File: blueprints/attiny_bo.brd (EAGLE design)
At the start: 36 x 20 mm, 8 parts, among them IC1 ATTiny85, J1 AVR_SPI_PRG_6NS

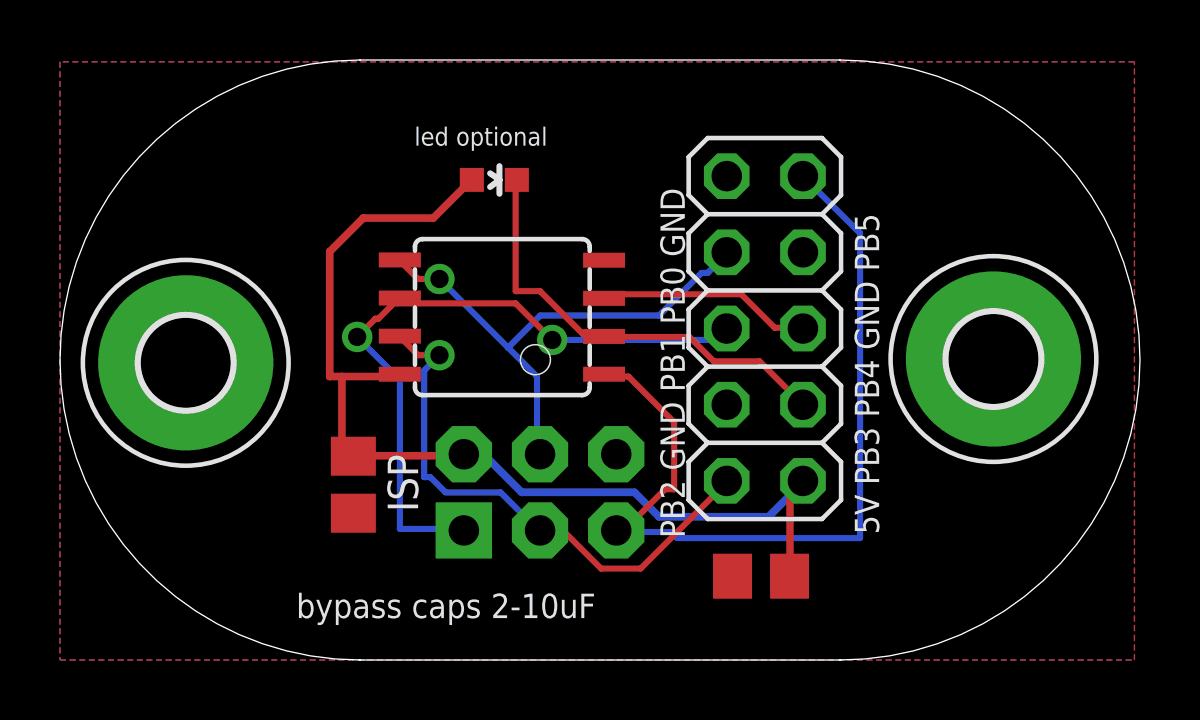
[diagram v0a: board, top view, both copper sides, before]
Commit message: rethought the signals to 5x2 header, tuned the mounting pad positions
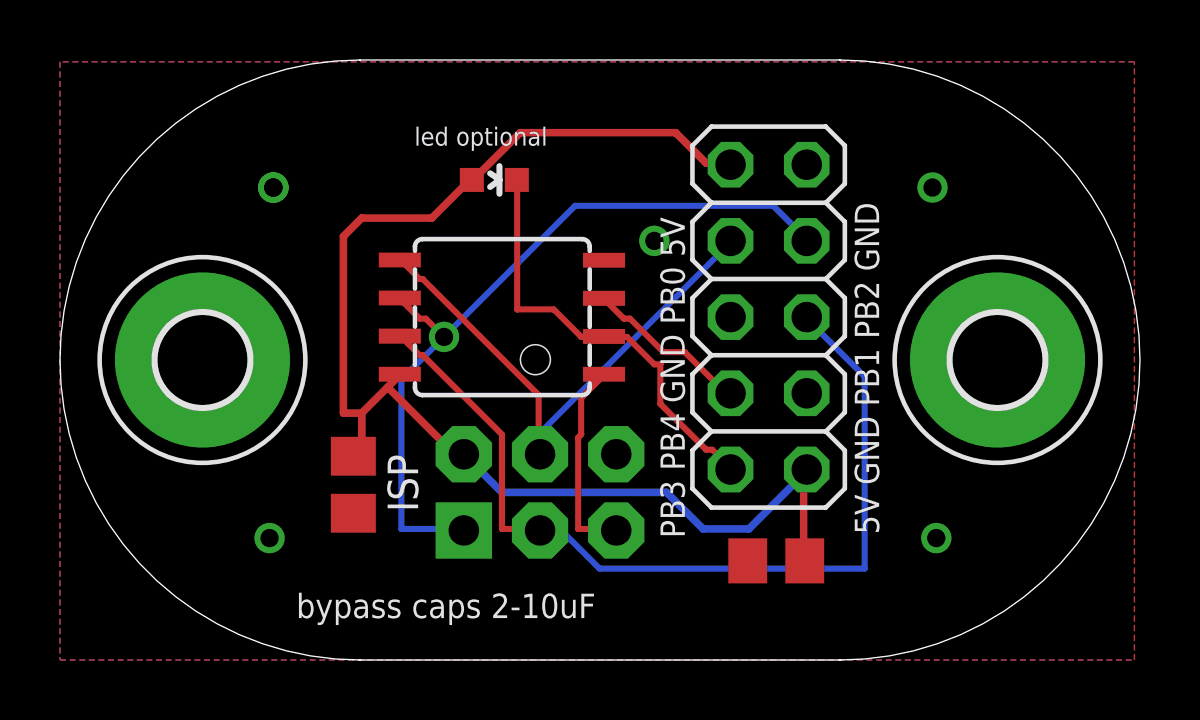
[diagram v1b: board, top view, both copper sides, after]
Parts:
- moved C2 0.72 mm to (23.9, 3.30)
- moved H1 0.57 mm to (4.75, 10.0)
- moved JP1 0.40 mm to (23.6, 11.4)
- moved H2 0.14 mm to (31.2, 10.0)
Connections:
- net +5V: now also JP1.1
- net GND: now also JP1.2, JP1.5, JP1.8; no longer JP1.1, JP1.4, JP1.7
- net PB1: now also JP1.4; no longer JP1.5
- net PB2: now also JP1.6; no longer JP1.9
- net PB3: now also JP1.9; no longer JP1.8
- net PB4: now also JP1.7; no longer JP1.6
- net PB5: no longer JP1.2
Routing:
- net PB5: track 28.9 -> 6.80 mm
- net PB2: track 18.5 -> 29.7 mm, vias 1 -> 0
- net +5V: track 35.4 -> 44.7 mm
- net PB1: track 23.0 -> 25.5 mm, vias 2 -> 1
- net PB4: track 7.15 -> 5.56 mm
- net PB0: track 17.5 -> 18.2 mm, vias 1 -> 0
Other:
- board text added: "5V GND PB1 PB2 GND"
- board text added: "PB3 PB4 GND PB0 5V"
- board text added: "PB5/Reset on ISP pin 5"
- board text removed: "5V PB3 PB4 GND PB5"
- board text removed: "PB2 GND PB1 PB0 GND"
